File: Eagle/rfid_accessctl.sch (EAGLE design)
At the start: 16 parts

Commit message: Start v1.2 board version
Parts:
- removed U$1: V_REG_LD1117VXX, SparkFun-PowerIC:V_REG_LD1117VXX
- added D1, D2: (no value), SparkFun-DiscreteSemi:DIODESMA
- added JMP1: 0R-JUMPB, jump-0r-smd:0R-JUMPB
- added Q1: IRLL014, Misc_Transistors:IRLL014
- added R6: (no value), SparkFun-Resistors:RESISTOR0805-RES
- added VR1: UA78M33CDCY, TI-UA78M33CDCY:UA78M33CDCY
- C1: value (none) -> 0.33uF; device SparkFun-Capacitors:10UF-25V-20%(PTH)KIT -> SparkFun-Capacitors:CAP0805
- C2: value (none) -> 0.1uF; device SparkFun-Capacitors:0.1UF-50V-20%(PTH)KIT-EZ -> SparkFun-Capacitors:CAP0805
- R5: value 470 -> 4.7k
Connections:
- new net RELAY_OP: D2.A, Q1.D1, RELAY_HEADER.1
- new net RELAY_PWR: D2.C, JMP1-0R.2, RELAY_HEADER.3
- net GND: now also C1.2, D1.A, LED_HEADER.3, Q1.S, R6.1, VR1.COM, VR1.COM_2; no longer C1.-, LED_HEADER.2, U$1.GND
- net PWR_IN: now also C1.1, D1.C, JMP1-0R.3, VR1.INPUT; no longer C2.1, RELAY_HEADER.3, U$1.IN
- net RELAY_CTL: now also Q1.G, R6.2; no longer RELAY_HEADER.1
- net VCC: now also C2.1, JMP1-0R.1, LED_HEADER.2, VR1.OUTPUT; no longer C1.+, LED_HEADER.3, U$1.OUT
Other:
- moved on the sheet: C2

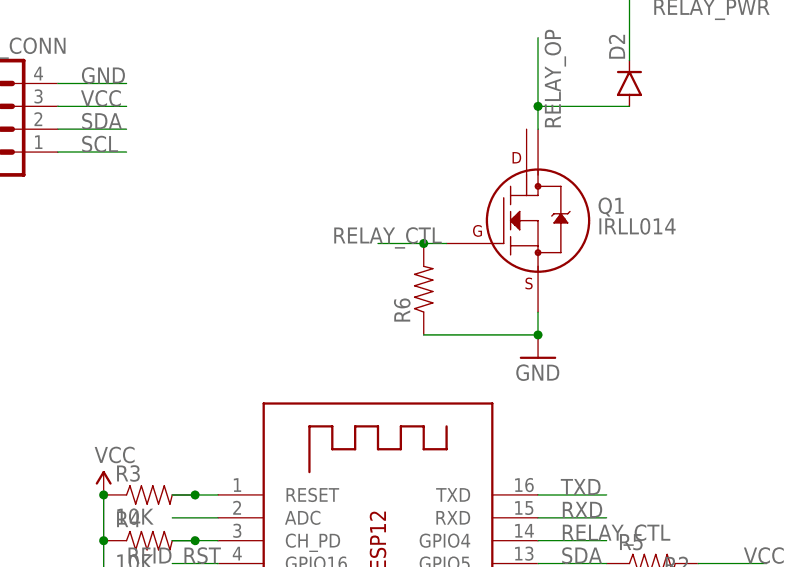
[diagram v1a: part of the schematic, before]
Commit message: Updates for 0603
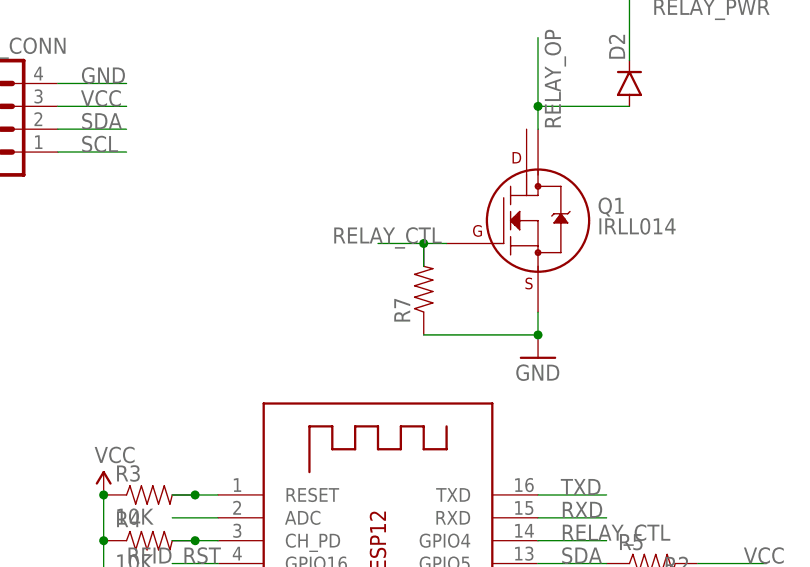
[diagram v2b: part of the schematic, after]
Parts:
- removed R6: (no value), SparkFun-Resistors:RESISTOR0805-RES
- added R7: (no value), SparkFun-Passives:RESISTOR0603-RES
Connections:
- net GND: now also R7.1; no longer R6.1
- net RELAY_CTL: now also R7.2; no longer R6.2
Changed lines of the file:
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@@
 <part name="D1" library="SparkFun-DiscreteSemi" deviceset="DIODE" device="SMA"/>
 <part name="D2" library="SparkFun-DiscreteSemi" deviceset="DIODE" device="SMA"/>
-<part name="R6" library="SparkFun-Resistors" deviceset="RESISTOR" device="0805-RES"/>
+<part name="R7" library="SparkFun-Passives" deviceset="RESISTOR" device="0603-RES"/>
 </parts>
 <sheets>
@@
 <instance part="D1" gate="G$1" x="27.94" y="40.64" rot="R90"/>
 <instance part="D2" gate="G$1" x="106.68" y="96.52" rot="R90"/>
-<instance part="R6" gate="G$1" x="83.82" y="73.66" rot="R90"/>
+<instance part="R7" gate="G$1" x="83.82" y="73.66" rot="R90"/>
 </instances>
 <busses>
@@
 <pinref part="GND2" gate="1" pin="GND"/>
 <wire x1="96.52" y1="68.58" x2="96.52" y2="71.12" width="0.1524" layer="91"/>
+<pinref part="R7" gate="G$1" pin="1"/>
+<wire x1="96.52" y1="68.58" x2="83.82" y2="68.58" width="0.1524" layer="91"/>
 <junction x="96.52" y="68.58"/>
-<pinref part="R6" gate="G$1" pin="1"/>
-<wire x1="96.52" y1="68.58" x2="83.82" y2="68.58" width="0.1524" layer="91"/>
 </segment>
 <segment>
@@
 <segment>
 <pinref part="Q1" gate="G$1" pin="G"/>
+<label x="73.66" y="78.74" size="1.778" layer="95"/>
 <wire x1="86.36" y1="78.74" x2="83.82" y2="78.74" width="0.1524" layer="91"/>
-<label x="73.66" y="78.74" size="1.778" layer="95"/>
-<pinref part="R6" gate="G$1" pin="2"/>
+<pinref part="R7" gate="G$1" pin="2"/>
 <wire x1="83.82" y1="78.74" x2="78.74" y2="78.74" width="0.1524" layer="91"/>
+<wire x1="83.82" y1="76.2" x2="83.82" y2="78.74" width="0.1524" layer="91"/>
 <junction x="83.82" y="78.74"/>
 </segment>

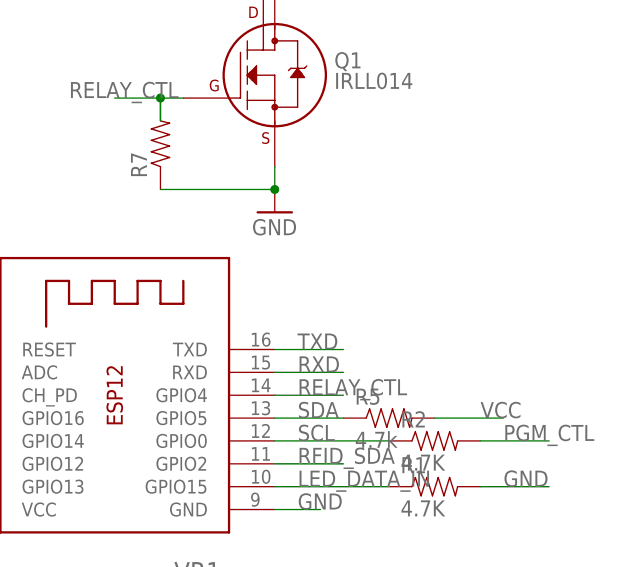
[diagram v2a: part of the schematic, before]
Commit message: Add DIP switches on serial lines (optional)
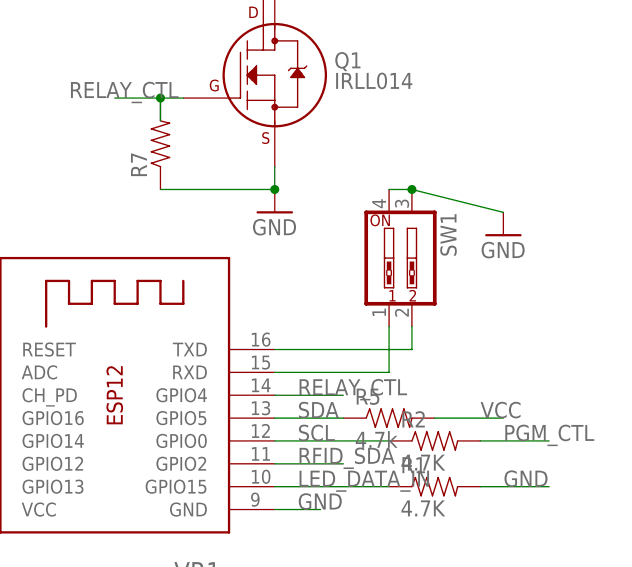
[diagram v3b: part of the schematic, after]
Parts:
- added SW1: (no value), SparkFun-Electromechanical:SW_DIP-2-SMT-HALFSIZE
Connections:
- net GND: now also SW1.3, SW1.4
- net RXD: now also SW1.1
- net TXD: now also SW1.2
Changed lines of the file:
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@@
 <part name="D2" library="SparkFun-DiscreteSemi" deviceset="DIODE" device="SMA"/>
 <part name="R7" library="SparkFun-Passives" deviceset="RESISTOR" device="0603-RES"/>
+<part name="SW1" library="SparkFun-Electromechanical" deviceset="SW_DIP-2" device="-SMT-HALFSIZE"/>
+<part name="GND3" library="SparkFun-Aesthetics" deviceset="GND" device=""/>
 </parts>
 <sheets>
@@
 <instance part="D2" gate="G$1" x="106.68" y="96.52" rot="R90"/>
 <instance part="R7" gate="G$1" x="83.82" y="73.66" rot="R90"/>
+<instance part="SW1" gate="G$1" x="111.76" y="60.96" rot="R270"/>
+<instance part="GND3" gate="1" x="121.92" y="63.5"/>
 </instances>
 <busses>
@@
 <label x="17.78" y="73.66" size="1.778" layer="95"/>
 </segment>
+<segment>
+<pinref part="SW1" gate="G$1" pin="4"/>
+<pinref part="SW1" gate="G$1" pin="3"/>
+<wire x1="109.22" y1="68.58" x2="111.76" y2="68.58" width="0.1524" layer="91"/>
+<wire x1="111.76" y1="68.58" x2="121.92" y2="66.04" width="0.1524" layer="91"/>
+<junction x="111.76" y="68.58"/>
+<pinref part="GND3" gate="1" pin="GND"/>
+</segment>
 </net>
 <net name="PWR_IN" class="0">
@@
 </segment>
 <segment>
+<pinref part="SW1" gate="G$1" pin="1"/>
+<wire x1="109.22" y1="53.34" x2="109.22" y2="48.26" width="0.1524" layer="91"/>
 <pinref part="X1" gate="G$1" pin="RXD"/>
-<label x="99.06" y="48.26" size="1.778" layer="95"/>
-<wire x1="96.52" y1="48.26" x2="104.14" y2="48.26" width="0.1524" layer="91"/>
+<wire x1="109.22" y1="48.26" x2="96.52" y2="48.26" width="0.1524" layer="91"/>
 </segment>
 </net>
@@
 <segment>
 <pinref part="X1" gate="G$1" pin="TXD"/>
-<wire x1="96.52" y1="50.8" x2="104.14" y2="50.8" width="0.1524" layer="91"/>
-<label x="99.06" y="50.8" size="1.778" layer="95"/>
-</segment>
-</net>
+<pinref part="SW1" gate="G$1" pin="2"/>
+<wire x1="96.52" y1="50.8" x2="111.76" y2="50.8" width="0.1524" layer="91"/>
+<wire x1="111.76" y1="50.8" x2="111.76" y2="53.34" width="0.1524" layer="91"/>
+</segment>
+</net>

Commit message: Final updates, as per mfr
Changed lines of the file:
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@@
 <?xml version="1.0" encoding="utf-8"?>
 <!DOCTYPE eagle SYSTEM "eagle.dtd">
-<eagle version="7.6.0">
+<eagle version="7.5.0">
 <drawing>
 <settings>
@@
 <instance part="R7" gate="G$1" x="83.82" y="73.66" rot="R90"/>
 <instance part="SW1" gate="G$1" x="111.76" y="60.96" rot="R270"/>
-<instance part="GND3" gate="1" x="121.92" y="63.5"/>
+<instance part="GND3" gate="1" x="121.92" y="66.04"/>
 </instances>
 <busses>
@@
 <pinref part="SW1" gate="G$1" pin="3"/>
 <wire x1="109.22" y1="68.58" x2="111.76" y2="68.58" width="0.1524" layer="91"/>
-<wire x1="111.76" y1="68.58" x2="121.92" y2="66.04" width="0.1524" layer="91"/>
+<wire x1="111.76" y1="68.58" x2="121.92" y2="68.58" width="0.1524" layer="91"/>
 <junction x="111.76" y="68.58"/>
 <pinref part="GND3" gate="1" pin="GND"/>
